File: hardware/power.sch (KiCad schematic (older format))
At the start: 0 parts

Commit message: Added latest printout
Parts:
- added J?: Vin, symbol Conn_01x02
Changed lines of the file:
@@
 Text HLabel 9250 2050 2    60   Output Italic 0
 3.3_OUT
+$Comp
+L Conn_01x02 J?
+U 1 1 5AE92ED9
+P 3300 3400
+F 0 "J?" H 3300 3500 50  0000 C CNN
+F 1 "Vin" H 3300 3200 50  0000 C CNN
+F 2 "" H 3300 3400 50  0001 C CNN
+F 3 "" H 3300 3400 50  0001 C CNN
+	1    3300 3400
+	1    0    0    -1
+$EndComp
 $EndSCHEMATC

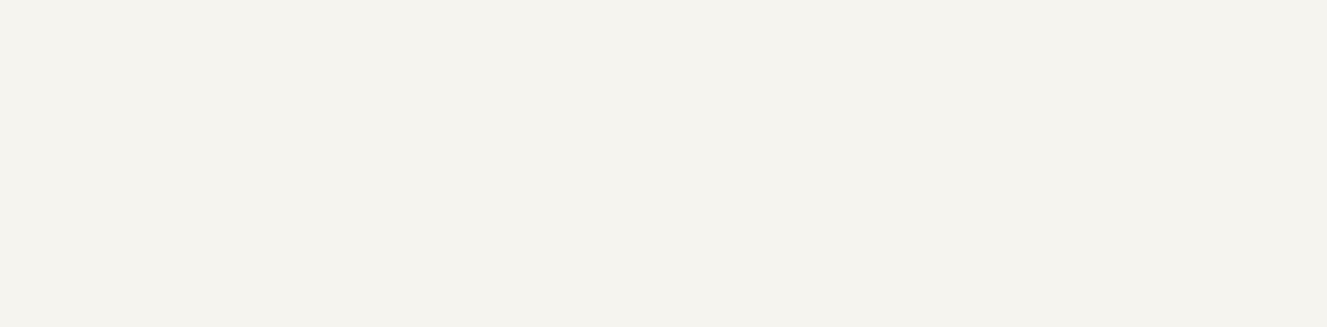
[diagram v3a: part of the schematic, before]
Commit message: Added notes for reverse current protection
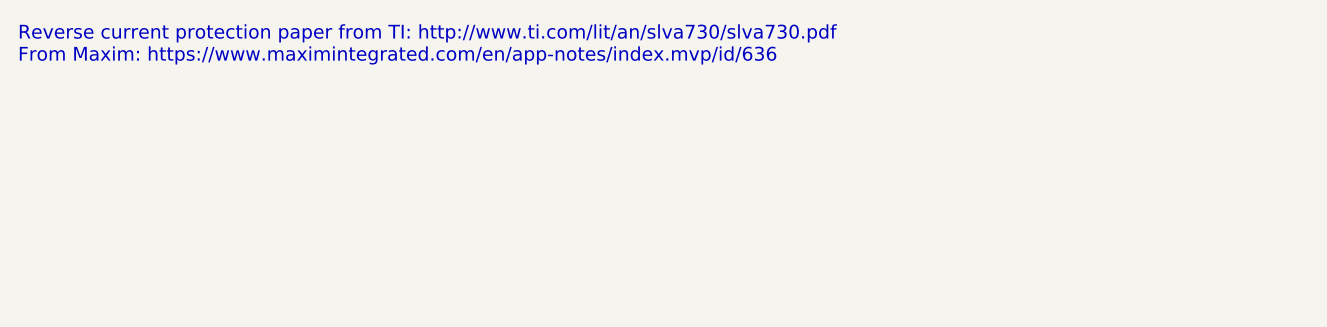
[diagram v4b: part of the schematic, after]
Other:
- note added: "Reverse current protection paper from TI: http://www.ti.com/lit/an/slva730/slva730.pdf\nFrom Maxim: https://www.maximintegrated.com/en/app-notes/index.mvp/id/636"
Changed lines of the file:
@@
 	1    0    0    -1
 $EndComp
+Text Notes 800  700  0    60   ~ 0
+Reverse current protection paper from TI: http://www.ti.com/lit/an/slva730/slva730.pdf\nFrom Maxim: https://www.maximintegrated.com/en/app-notes/index.mvp/id/636
 $EndSCHEMATC
